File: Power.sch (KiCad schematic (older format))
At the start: 23 parts, among them Q1 PMOS, U6 MCP73831-2-OT, U7 TPS737xx

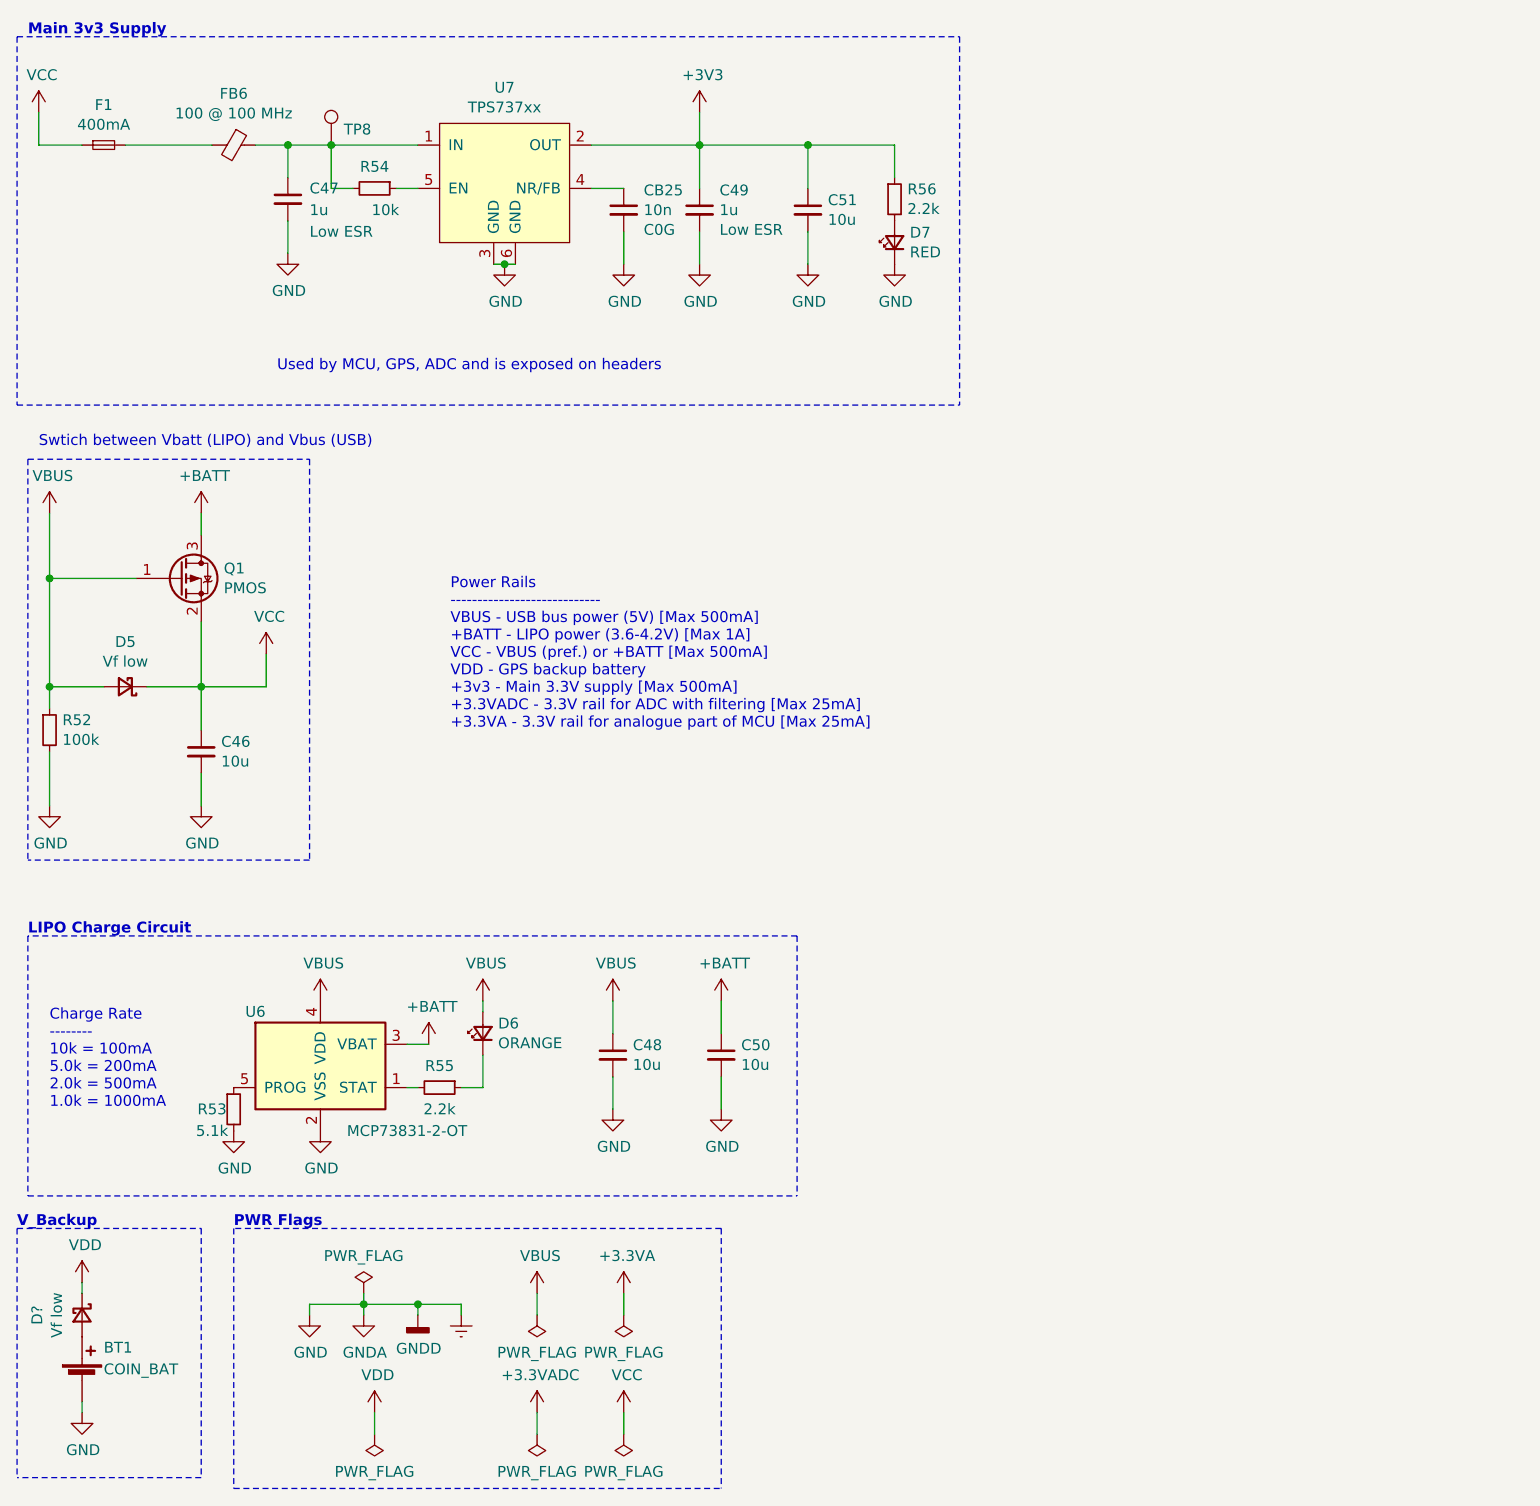
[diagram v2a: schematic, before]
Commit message: Change Mic Preamp
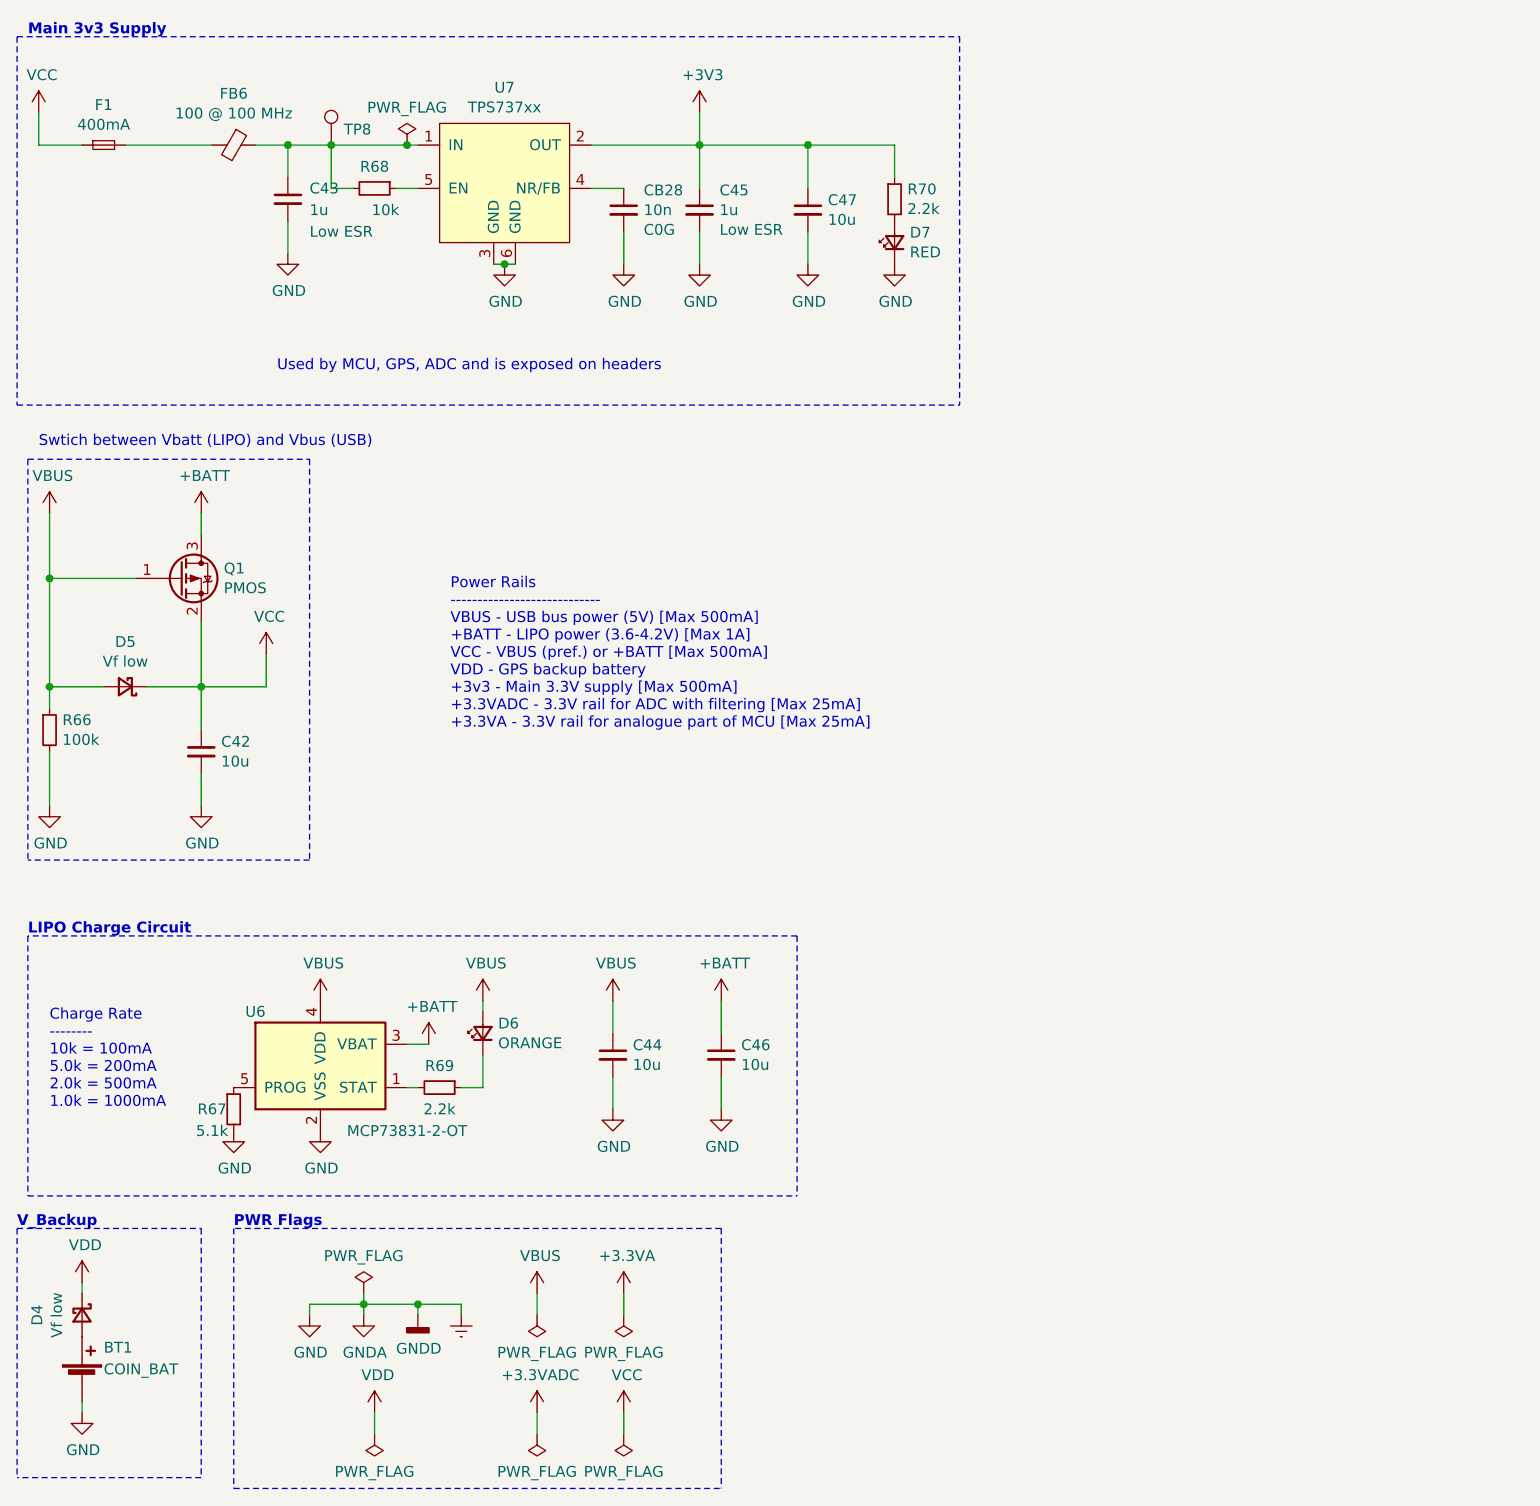
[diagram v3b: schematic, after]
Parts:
- C42: renamed from C46; MPN (none) -> C0805C106K9PACTU; Mfr. (none) -> KEMET
- C44: renamed from C48; MPN (none) -> C0805C106K9PACTU; Mfr. (none) -> KEMET
- C46: renamed from C50; MPN (none) -> C0805C106K9PACTU; Mfr. (none) -> KEMET
- C47: renamed from C51; MPN (none) -> C0805C106K9PACTU; Mfr. (none) -> KEMET
- CB28: renamed from CB25; MPN (none) -> C0603C103J5RACTU; Mfr. (none) -> KEMET
- R69: renamed from R55; MPN (none) -> RC0603FR-072K2L; Mfr. (none) -> Yageo
- R70: renamed from R56; MPN (none) -> RC0603FR-072K2L; Mfr. (none) -> Yageo
- gave numbers to parts that had none: 1
- renumbered C47 to C43, C49 to C45, R52 to R66, R53 to R67, R54 to R68

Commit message: Fix BOM ref
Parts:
- R68: MPN (none) -> RC0603JR-0710KL; Mfr. (none) -> Yageo
- U6: MPN MCP73831-2-OT -> MCP73831T-2ACI/OT
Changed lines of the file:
@@
 $Descr A4 11693 8268
 encoding utf-8
-Sheet 13 15
+Sheet 15 17
 Title "Kleinvoet"
 Date "2020-06-11"
@@
 F 2 "Resistor_SMD:R_0603_1608Metric_Pad1.05x0.95mm_HandSolder" H 5200 1650 50  0001 C CNN
 F 3 "~" H 5200 1650 50  0001 C CNN
+F 4 "RC0603JR-0710KL" H 5200 1650 50  0001 C CNN "MPN"
+F 5 "Yageo" H 5200 1650 50  0001 C CNN "Mfr."
 	1    5200 1650
 	0    1    1    0
@@
 F 3 "http://ww1.microchip.com/downloads/en/DeviceDoc/20001984g.pdf" H 4800 5650 50  0001 C CNN
 F 4 "Microchip" H 4950 5700 50  0001 C CNN "Mfr."
-F 5 "MCP73831-2-OT" H 4950 5700 50  0001 C CNN "MPN"
+F 5 "MCP73831T-2ACI/OT" H 4950 5700 50  0001 C CNN "MPN"
 	1    4950 5700
 	1    0    0    -1

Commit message: PCB Layout Checkpoint
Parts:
- renumbered C42 to C58, C43 to C59, C44 to C60, C45 to C61, C46 to C62, C47 to C63, CB28 to CB38, FB6 to FB8, R66 to R84, R67 to R85, R68 to R86, R69 to R87, R70 to R88, TP8 to TP14, U6 to U8, U7 to U9
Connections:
- net Earth: no longer BT1.2 (-), C58.2, C59.2, C60.2, C61.2, C62.2, C63.2, CB38.2, D7.1 (K), R84.2, R85.2, U8.2 (VSS), U9.3 (GND), U9.6 (GND)
- new net GND: BT1.2 (-), C58.2, C59.2, C60.2, C61.2, C62.2, C63.2, CB38.2, D7.1 (K), R84.2, R85.2, U8.2 (VSS), U9.3 (GND), U9.6 (GND)

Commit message: Major Commit with Final PCB Design
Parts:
- removed C61: 1u, Capacitor_SMD:C_0603_1608Metric_Pad1.05x0.95mm_HandSolder, symbol Device:C_Small
- removed U9: TPS737xx, grootvoet:TPS737, symbol grootvoet:TPS737xx
- added U9: TPS73733QDRBRQ1, grootvoet:Texas_DRB0008A, symbol grootvoet:TPS73733QDRBRQ1
- C59: value 1u -> 10u; footprint Capacitor_SMD:C_0603_1608Metric_Pad1.05x0.95mm_HandSolder -> Capacitor_SMD:C_0805_2012Metric_Pad1.15x1.40mm_HandSolder; MPN C0603C105K8RACTU -> C0805C106K9PACTU; Notes Low ESR -> (none)
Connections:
- net +3V3: now also U9.1 (OUT)
- net GND: now also U9.4 (GND), U9.9 (GND)
- net at C59.1, FB8.1, R86.2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: now also U9.8 (IN)
- net at CB38.1: now also U9.3 (NR/FB)
- net at R86.1: now also U9.5 (EN)
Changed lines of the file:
@@
-	1    0    0    -1
-$EndComp
-$Comp
-L grootvoet:TPS737xx U9
-U 1 1 5EEEA2A4
-P 5800 1550
-F 0 "U9" H 5800 1915 50  0000 C CNN
-F 1 "TPS737xx" H 5800 1824 50  0000 C CNN
-F 2 "grootvoet:TPS737" H 6050 1800 50  0001 C CNN
-F 3 "" H 6050 1800 50  0001 C CNN
-F 4 "TPS73733DCQR" H 5800 1550 50  0001 C CNN "MPN"
-F 5 "Texas Instruments" H 5800 1550 50  0001 C CNN "Mfr."
-	1    5800 1550
 	1    0    0    -1
 $EndComp
@@
 $EndComp
 Wire Wire Line
-	5750 2000 5800 2000
-Connection ~ 5800 2000
-Wire Wire Line
-	5800 2000 5850 2000
-$Comp
-L Device:C_Small C59
-U 1 1 5EEF11C8
-P 4800 1700
-F 0 "C59" H 4900 1750 50  0000 L CNN
-F 1 "1u" H 4900 1650 50  0000 L CNN
-F 2 "Capacitor_SMD:C_0603_1608Metric_Pad1.05x0.95mm_HandSolder" H 4800 1700 50  0001 C CNN
-F 3 "~" H 4800 1700 50  0001 C CNN
-F 4 "Low ESR" H 4900 1550 50  0000 L CNN "Notes"
-F 5 "C0603C105K8RACTU" H 4800 1700 50  0001 C CNN "MPN"
-F 6 "KEMET" H 4800 1700 50  0001 C CNN "Mfr."
-	1    4800 1700
-	1    0    0    -1
-$EndComp
-Wire Wire Line
 	4700 3950 4400 3950
 $Comp
@@
 	6350 1650 6200 1650
 $Comp
-L Device:C_Small C61
-U 1 1 5EEF3784
-P 6700 1750
-F 0 "C61" H 6792 1841 50  0000 L CNN
-F 1 "1u" H 6792 1750 50  0000 L CNN
-F 2 "Capacitor_SMD:C_0603_1608Metric_Pad1.05x0.95mm_HandSolder" H 6700 1750 50  0001 C CNN
-F 3 "~" H 6700 1750 50  0001 C CNN
-F 4 "Low ESR" H 6792 1659 50  0000 L CNN "Notes"
-F 5 "C0603C105K8RACTU" H 6700 1750 50  0001 C CNN "MPN"
-F 6 "KEMET" H 6700 1750 50  0001 C CNN "Mfr."
-	1    6700 1750
-	1    0    0    -1
-$EndComp
-$Comp
 L Device:C_Small C63
 U 1 1 5EEF3E13
@@
 	6200 1450 6700 1450
 Wire Wire Line
-	6700 1450 6700 1650
-Wire Wire Line
 	6700 1450 7200 1450
 Wire Wire Line
 	7200 1450 7200 1650
 Connection ~ 6700 1450
-$Comp
-L power:GND #PWR0115
-U 1 1 5EEF8C9F
-P 6700 2000
-F 0 "#PWR0115" H 6700 1750 50  0001 C CNN
-F 1 "GND" H 6705 1827 50  0000 C CNN
-F 2 "" H 6700 2000 50  0001 C CNN
-F 3 "" H 6700 2000 50  0001 C CNN
-	1    6700 2000
-	1    0    0    -1
-$EndComp
 $Comp
 L power:GND #PWR0118
@@
 Wire Wire Line
 	7200 2000 7200 1850
-Wire Wire Line
-	6700 2000 6700 1850
 Wire Wire Line
 	6350 1850 6350 2000
@@
 Wire Wire Line
 	5600 6750 5600 6850
+$Comp
+L grootvoet:TPS73733QDRBRQ1 U9
+U 1 1 5F155C9C
+P 5800 1550
+F 0 "U9" H 5800 1915 50  0000 C CNN
+F 1 "TPS73733QDRBRQ1" H 5800 2000 50  0000 C CNN
+F 2 "grootvoet:Texas_DRB0008A" H 6050 1800 50  0001 C CNN
+F 3 "" H 6050 1800 50  0001 C CNN
+F 4 "TPS73733QDRBRQ1" H 5800 1550 50  0001 C CNN "MPN"
+F 5 "Texas Instruments" H 5800 1550 50  0001 C CNN "Mfr."
+	1    5800 1550
+	1    0    0    -1
+$EndComp
+$Comp
+L Device:C_Small C59
+U 1 1 5F15E5E6
+P 4800 1700
+F 0 "C59" H 4892 1746 50  0000 L CNN
+F 1 "10u" H 4892 1655 50  0000 L CNN
+F 2 "Capacitor_SMD:C_0805_2012Metric_Pad1.15x1.40mm_HandSolder" H 4800 1700 50  0001 C CNN
+F 3 "~" H 4800 1700 50  0001 C CNN
+F 4 "C0805C106K9PACTU" H 4800 1700 50  0001 C CNN "MPN"
+F 5 "KEMET" H 4800 1700 50  0001 C CNN "Mfr."
+	1    4800 1700
+	1    0    0    -1
+$EndComp
 $EndSCHEMATC

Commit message: Merge 'feature/mic-board'
Split out Sensor_board to own project for easier panelising later.
Allows also for better independent development.

Squashed commit of the following:
===============================================
commit 5c89ddf7514428c762fb7c211bc44fe947092eb1
Author: CM Geldenhuys <20198329@sun.ac.za>
Date:   Wed Oct 21 14:34:31 2020 +0200

    Add emblem

commit bbe0a53b49b0ec3aa4e2f65424c556ce99509fe4
Author: CM Geldenhuys <20198329@sun.ac.za>
Date:   Wed Oct 21 11:03:40 2020 +0200

    Misc.

commit b3172de48a622d4a7c8e9fb13a381d32a0990437
Author: CM Geldenhuys <20198329@sun.ac.za>
Date:   Wed Oct 21 08:26:42 2020 +0200

    Update BOM

commit e4c5b39694adfe3b823840b4cd3bc00d306b52fc
Author: CM Geldenhuys <20198329@sun.ac.za>
Date:   Wed Oct 21 07:26:34 2020 +0200

    Update Footprint & part num.

commit 6125562d7501cc555d98682860bdd64678a2fa40
Author: CM Geldenhuys <20198329@sun.ac.za>
Date:   Tue Oct 20 15:41:10 2020 +0200

    Misc. TODOs

commit 1431b8ace7af2c4960b7d9361ce6fcca694d3a38
Author: CM Geldenhuys <20198329@sun.ac.za>
Date:   Tue Oct 20 11:22:04 2020 +0200

    Update passives (fuse + Vsense)

commit 8105b403ec058cf7267c739b2e244ad8880c475f
Author: CM Geldenhuys <20198329@sun.ac.za>
Date:   Tue Oct 20 11:02:06 2020 +0200

    Flip GPS labels

commit f34b34dca70ce235e33188df7f6c69707ad79c9c
Author: CM Geldenhuys <20198329@sun.ac.za>
Date:   Tue Oct 20 10:58:45 2020 +0200

    Swap out ST-Link Conn

commit 1669b3f99c1cffa6c87811843550b346cfb9297e
Author: CM Geldenhuys <20198329@sun.ac.za>
Date:   Tue Oct 20 09:57:40 2020 +0200

    Update Sch with new compensation

commit dde033bb3cbd48a104931da2f1a7f681a8f96ac4
Author: CM Geldenhuys <20198329@sun.ac.za>
Date:   Tue Oct 20 09:55:04 2020 +0200

    Compensate for preamp loading on ADC driver

commit 2ddbd04fb1deccaa72131771362207bd14115936
Author: CM Geldenhuys <20198329@sun.ac.za>
Date:   Tue Oct 20 09:38:09 2020 +0200

    Compensate for buffer output impedance

commit 2f74ea7d6b171bacb6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
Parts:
- CB38: footprint Capacitor_SMD:C_0603_1608Metric_Pad1.05x0.95mm_HandSolder -> Capacitor_SMD:C_0603_1608Metric_Pad1.08x0.95mm_HandSolder
- F1: MPN 0686F0500-01 -> 0ZCM0020FF2G
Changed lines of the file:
@@
 $Descr A4 11693 8268
 encoding utf-8
-Sheet 15 17
+Sheet 11 13
 Title "Kleinvoet"
 Date "2020-06-11"
@@
 F 0 "CB38" H 6442 1841 50  0000 L CNN
 F 1 "10n" H 6442 1750 50  0000 L CNN
-F 2 "Capacitor_SMD:C_0603_1608Metric_Pad1.05x0.95mm_HandSolder" H 6350 1750 50  0001 C CNN
+F 2 "Capacitor_SMD:C_0603_1608Metric_Pad1.08x0.95mm_HandSolder" H 6350 1750 50  0001 C CNN
 F 3 "~" H 6350 1750 50  0001 C CNN
 F 4 "C0G" H 6442 1659 50  0000 L CNN "Notes"
@@
 F 2 "Fuse:Fuse_0603_1608Metric_Pad1.05x0.95mm_HandSolder" H 3950 1450 50  0001 C CNN
 F 3 "~" H 3950 1450 50  0001 C CNN
-F 4 "0686F0500-01" H 3950 1450 50  0001 C CNN "MPN"
+F 4 "0ZCM0020FF2G" H 3950 1450 50  0001 C CNN "MPN"
 F 5 "Bel Fuse" H 3950 1450 50  0001 C CNN "Mfr."
 	1    3950 1450
